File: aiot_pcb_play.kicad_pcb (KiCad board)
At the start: 4 copper layers, 56 x 85 mm, 15 parts, among them J1 10_pin_swd_connector, J2 Tag-Connect, U1 BC833M, U2 16_pin_header, U3 ITM-DYPA-B-02

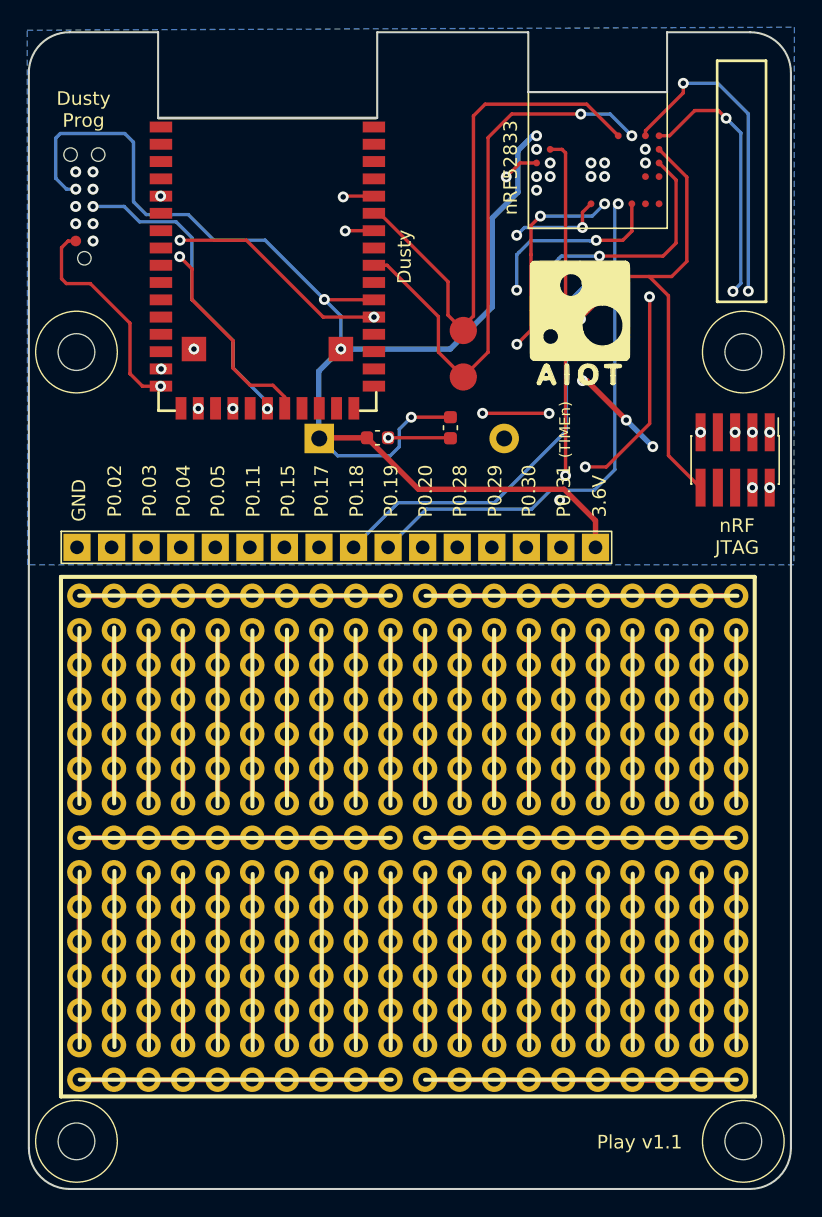
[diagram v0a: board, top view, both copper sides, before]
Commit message: Finished the design of the AIOT Play v1.2 addressing #5 and #6
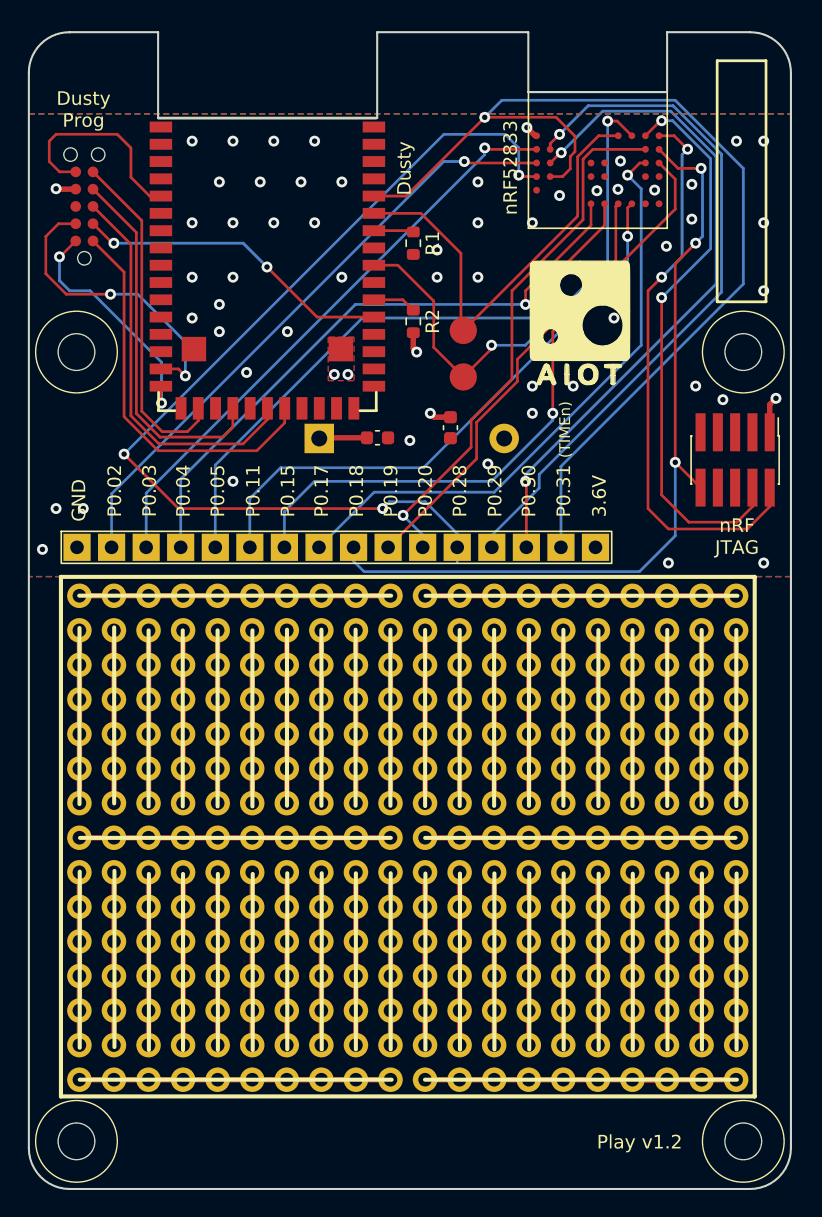
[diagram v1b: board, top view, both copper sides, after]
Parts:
- added G***: LOGO, AIOT_logo:falco_logo, B.Cu at (153.0, 61.0)
- added G***: LOGO, AIOT_logo:inria_logo, B.Cu at (152.0, 69.0)
- added R1: 100k, Resistor_SMD:R_0603_1608Metric, F.Cu at (153.2, 65.5)
- added R2: 100k, Resistor_SMD:R_0603_1608Metric, F.Cu at (153.2, 71.2)
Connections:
- U3 pad 33: VDD -> Net-(U3-UART_RX_RTSN)
- U3 pad 37: GND -> Net-(U3-UART_TX_CTSN)
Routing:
- net VDD: track 131.5 -> 11.8 mm, vias 6 -> 7
- net Net-(U1-P028): track 30.2 -> 71.9 mm, vias 1 -> 3
- net Net-(U1-P017): track 71.7 -> 44.4 mm, vias 5 -> 1
- net P0.31: track 50.0 -> 77.0 mm, vias 2 -> 1
- net Net-(U1-P020): track 60.7 -> 39.5 mm, vias 3 -> 1
- net Net-(U1-P029): track 34.1 -> 51.5 mm, vias 2 -> 1
- net GND: track 16.9 -> 0.00 mm, vias 16 -> 53
- net Net-(U1-P030): track 33.0 -> 49.7 mm, vias 1 -> 2
- net Net-(J2-IPCS_SSn): track 22.2 -> 28.6 mm, vias 2 -> 0
- net Net-(U1-P019): track 38.7 -> 32.2 mm, vias 1 -> 0
- net Net-(U1-P010): track 39.6 -> 33.2 mm
- net Net-(J2-UARTC0_TX): track 16.2 -> 22.2 mm
- net Net-(J2-IPCS__SCK): track 23.1 -> 29.0 mm, vias 2 -> 0
- net Net-(U1-P003): track 48.4 -> 43.5 mm
- net Net-(U1-P011): track 47.7 -> 43.0 mm, vias 2 -> 1
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- added copper zone on F.Cu, net GND
- added copper zone on In1.Cu, net GND
- added copper zone on F.Cu, net VDD
- added copper zone on In2.Cu, net VDD
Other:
- board text added: "Play v1.2"
- board text removed: "Play v1.1"

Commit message: #4 silkscreen changed p0.19->p1.09
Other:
- board text added: "P1.09"
- board text removed: "P0.19"
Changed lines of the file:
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@@
   (net 26 "Net-(U1-P004)")
   (net 27 "Net-(U1-P005)")
-  (net 28 "Net-(U1-P019)")
+  (net 28 "Net-(U1-P109)")
   (net 29 "Net-(U1-P011)")
   (net 30 "unconnected-(U1-VDDH-Pad13)")
@@
       (net 27 "Net-(U1-P005)") (pinfunction "P005") (pintype "input"))
     (pad "11" smd circle (at 1.5 0.2) (size 0.5 0.5) (layers "F.Cu" "F.Paste" "F.Mask")
-      (net 28 "Net-(U1-P019)") (pinfunction "P019") (pintype "input"))
+      (net 28 "Net-(U1-P109)") (pinfunction "P109") (pintype "input"))
     (pad "12" smd circle (at 2.5 0.2) (size 0.5 0.5) (layers "F.Cu" "F.Paste" "F.Mask")
       (net 29 "Net-(U1-P011)") (pinfunction "P011") (pintype "input"))
@@
       (net 7 "Net-(J1-nRESET)") (pinfunction "9") (pintype "input"))
     (pad "10" thru_hole rect (at 3.82 0.025) (size 2 2) (drill 1) (layers "*.Cu" "*.Mask")
-      (net 28 "Net-(U1-P019)") (pinfunction "10") (pintype "input"))
+      (net 28 "Net-(U1-P109)") (pinfunction "10") (pintype "input"))
     (pad "11" thru_hole rect (at 6.36 0.025) (size 2 2) (drill 1) (layers "*.Cu" "*.Mask")
       (net 36 "Net-(U1-P020)") (pinfunction "11") (pintype "input"))
@@
     (effects (font (size 1 1) (thickness 0.2)))
   )
-  (gr_text "P0.19" (at 151.61 83.71 90) (layer "F.SilkS")
+  (gr_text "P1.09" (at 151.61 83.71 90) (layer "F.SilkS")
     (effects (font (size 1 1) (thickness 0.2)))
   )
